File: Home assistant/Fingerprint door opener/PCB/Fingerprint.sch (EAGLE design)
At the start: 12 parts, among them K1 SNR03012, T2 BC337, X1 2PIN_5MM_TERMINAL, X2 3PIN_5MM_TERMINAL, X3 2PIN_5MM_TERMINAL, X4 0446200002

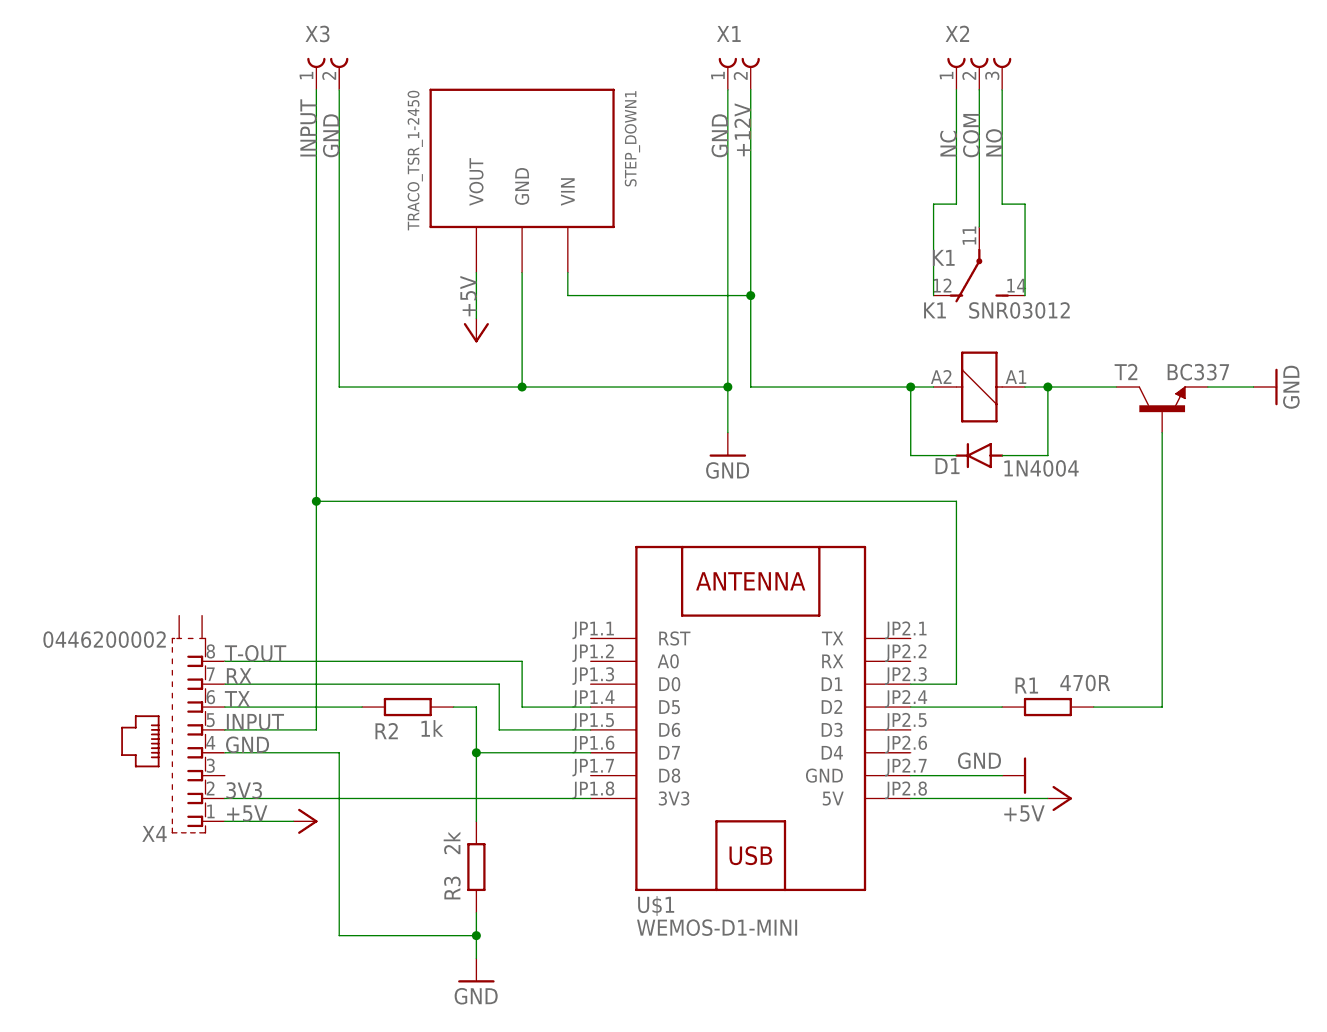
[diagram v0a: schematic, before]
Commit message: Fingerprint sensor reset function
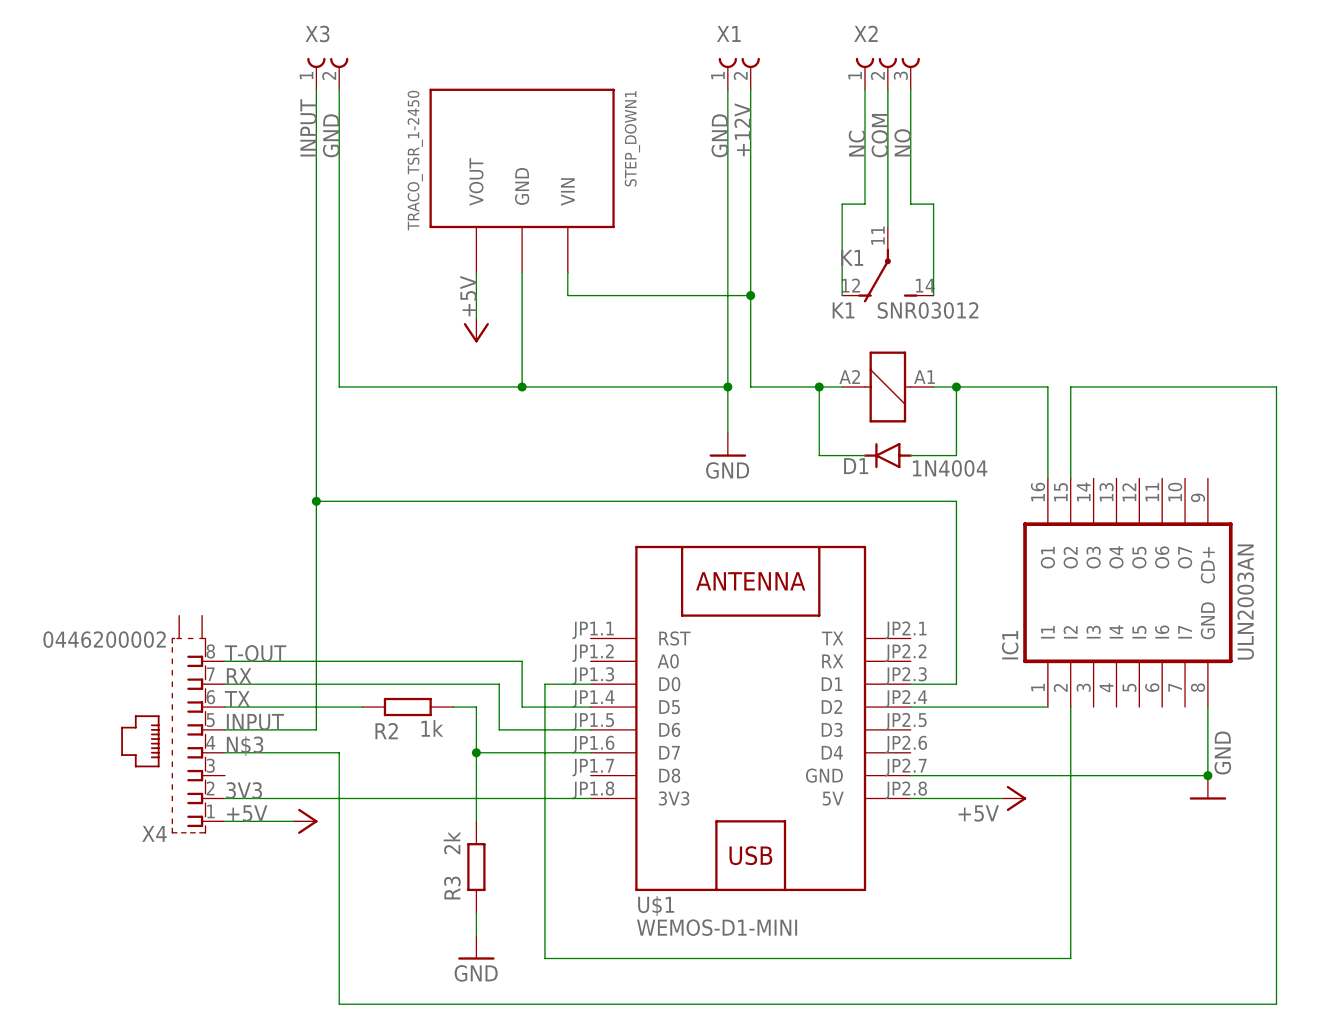
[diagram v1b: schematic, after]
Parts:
- removed R1: 470R, rcl:R-EU_0207/10
- removed T2: BC337, transistor:BC337IN_LINE
- added IC1: ULN2003AN, ULN:ULN2003AN
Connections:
- new net N$2: IC1.I2, U$1.D0
- net GND: now also IC1.GND; no longer T2.E, X4.4
- net N$1: now also IC1.O1; no longer T2.C
- net N$16: now also IC1.I1; no longer R1.1
- net N$3: now also IC1.O2, X4.4; no longer R1.2, T2.B
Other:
- moved on the sheet: D1, K1, X2
